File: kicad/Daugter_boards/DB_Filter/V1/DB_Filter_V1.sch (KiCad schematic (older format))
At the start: 4 parts, among them P1 CONN_01X19

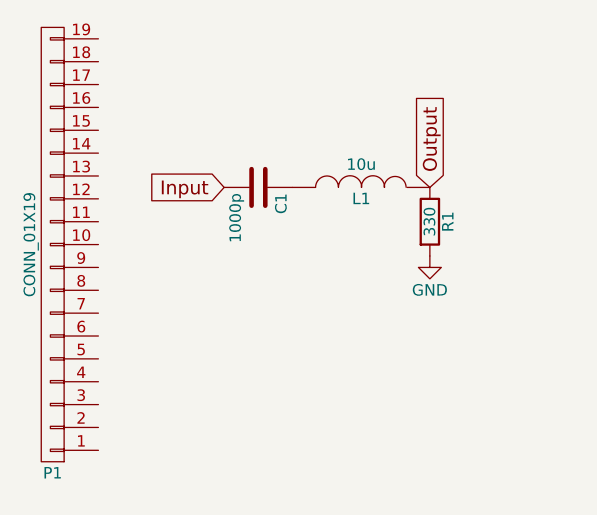
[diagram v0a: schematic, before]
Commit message: adding DB_Filter
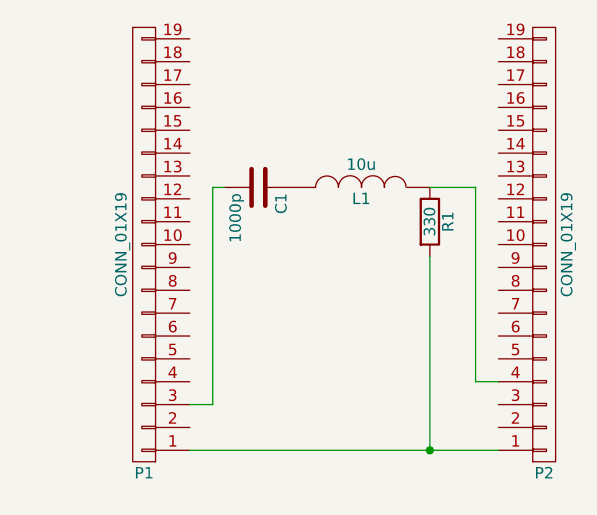
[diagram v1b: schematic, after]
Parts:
- added P2: CONN_01X19, symbol CONN_01X19
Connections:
- net GND is gone; now on an unnamed net: R1.2
- net Input is gone; now on an unnamed net: C1.2
- net at P1.1 (P1): now also P2.1 (P1)
- net Output: no longer names the net of L1.1, R1.1
- net Output: now also P2.4 (P4)
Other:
- moved on the sheet: P1
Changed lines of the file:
@@
 LIBS:valves
 LIBS:echopen
+LIBS:DB_Filter_V1-cache
 EELAYER 25 0
 EELAYER END
@@
 $EndComp
 $Comp
-L GND #PWR1
-U 1 1 57A4BBE1
-P 5350 3450
-F 0 "#PWR1" H 5350 3200 50  0001 C CNN
-F 1 "GND" H 5350 3300 50  0000 C CNN
-F 2 "" H 5350 3450 50  0000 C CNN
-F 3 "" H 5350 3450 50  0000 C CNN
-	1    5350 3450
-	1    0    0    -1
-$EndComp
-Text GLabel 4450 3150 0    60   Input ~ 0
-Input
-Text GLabel 5350 3150 1    60   Input ~ 0
-Output
-$Comp
 L CONN_01X19 P1
 U 1 1 57A84EF6
-P 3700 3400
-F 0 "P1" H 3700 4400 50  0000 C CNN
-F 1 "CONN_01X19" V 3800 3400 50  0000 C CNN
-F 2 "" H 3700 3400 50  0000 C CNN
-F 3 "" H 3700 3400 50  0000 C CNN
-	1    3700 3400
+P 4100 3400
+F 0 "P1" H 4100 4400 50  0000 C CNN
+F 1 "CONN_01X19" V 4200 3400 50  0000 C CNN
+F 2 "" H 4100 3400 50  0000 C CNN
+F 3 "" H 4100 3400 50  0000 C CNN
+	1    4100 3400
 	-1   0    0    1
 $EndComp
+$Comp
+L CONN_01X19 P2
+U 1 1 57A89932
+P 5850 3400
+F 0 "P2" H 5850 4400 50  0000 C CNN
+F 1 "CONN_01X19" V 5950 3400 50  0000 C CNN
+F 2 "" H 5850 3400 50  0000 C CNN
+F 3 "" H 5850 3400 50  0000 C CNN
+	1    5850 3400
+	1    0    0    1
+$EndComp
+Wire Wire Line
+	4300 4300 5650 4300
+Wire Wire Line
+	5350 3450 5350 4300
+Connection ~ 5350 4300
+Wire Wire Line
+	5350 3150 5550 3150
+Wire Wire Line
+	5550 3150 5550 4000
+Wire Wire Line
+	4400 3150 4400 4100
+Wire Wire Line
+	4400 3150 4450 3150
+Wire Wire Line
+	5550 4000 5650 4000
+Wire Wire Line
+	4400 4100 4300 4100
 $EndSCHEMATC

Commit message: adding DB_Filter
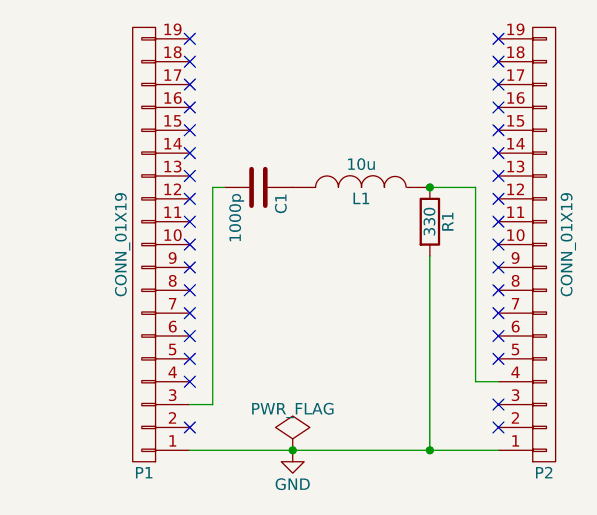
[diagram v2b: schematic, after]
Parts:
- C1: footprint (none) -> Capacitors_ThroughHole:C_Disc_D6_P5
- L1: footprint (none) -> Inductors:INDUCTOR_V
- P1, P2: footprint (none) -> Socket_Strips:Socket_Strip_Straight_1x19
- R1: footprint (none) -> Resistors_ThroughHole:Resistor_Horizontal_RM7mm
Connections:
- net GND: now reaches P1.1 (P1), P2.1 (P1), R1.2
- no-connect marks 0 -> 34
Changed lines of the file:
@@
 F 0 "C1" H 4625 3250 50  0000 L CNN
 F 1 "1000p" H 4625 3050 50  0000 L CNN
-F 2 "" H 4638 3000 50  0000 C CNN
+F 2 "Capacitors_ThroughHole:C_Disc_D6_P5" H 4638 3000 50  0001 C CNN
 F 3 "" H 4600 3150 50  0000 C CNN
 	1    4600 3150
@@
 F 0 "L1" V 5000 3150 50  0000 C CNN
 F 1 "10u" V 5150 3150 50  0000 C CNN
-F 2 "" H 5050 3150 50  0000 C CNN
+F 2 "Inductors:INDUCTOR_V" H 5050 3150 50  0001 C CNN
 F 3 "" H 5050 3150 50  0000 C CNN
 	1    5050 3150
@@
 F 0 "R1" V 5430 3300 50  0000 C CNN
 F 1 "330" V 5350 3300 50  0000 C CNN
-F 2 "" V 5280 3300 50  0000 C CNN
+F 2 "Resistors_ThroughHole:Resistor_Horizontal_RM7mm" V 5280 3300 50  0001 C CNN
 F 3 "" H 5350 3300 50  0000 C CNN
 	1    5350 3300
@@
 F 0 "P1" H 4100 4400 50  0000 C CNN
 F 1 "CONN_01X19" V 4200 3400 50  0000 C CNN
-F 2 "" H 4100 3400 50  0000 C CNN
+F 2 "Socket_Strips:Socket_Strip_Straight_1x19" H 4100 3400 50  0001 C CNN
 F 3 "" H 4100 3400 50  0000 C CNN
 	1    4100 3400
@@
 F 0 "P2" H 5850 4400 50  0000 C CNN
 F 1 "CONN_01X19" V 5950 3400 50  0000 C CNN
-F 2 "" H 5850 3400 50  0000 C CNN
+F 2 "Socket_Strips:Socket_Strip_Straight_1x19" H 5850 3400 50  0001 C CNN
 F 3 "" H 5850 3400 50  0000 C CNN
 	1    5850 3400
@@
 Wire Wire Line
 	4400 4100 4300 4100
+Connection ~ 5350 3150
+NoConn ~ 4300 2500
+NoConn ~ 4300 2600
+NoConn ~ 4300 2700
+NoConn ~ 4300 2800
+NoConn ~ 4300 2900
+NoConn ~ 4300 3000
+NoConn ~ 4300 3100
+NoConn ~ 4300 3200
+NoConn ~ 4300 3300
+NoConn ~ 4300 3400
+NoConn ~ 4300 3500
+NoConn ~ 4300 3600
+NoConn ~ 4300 3700
+NoConn ~ 4300 3800
+NoConn ~ 4300 3900
+NoConn ~ 4300 4000
+NoConn ~ 4300 4200
+NoConn ~ 5650 2500
+NoConn ~ 5650 2600
+NoConn ~ 5650 2700
+NoConn ~ 5650 2800
+NoConn ~ 5650 2900
+NoConn ~ 5650 3000
+NoConn ~ 5650 3100
+NoConn ~ 5650 3200
+NoConn ~ 5650 3300
+NoConn ~ 5650 3400
+NoConn ~ 5650 3500
+NoConn ~ 5650 3600
+NoConn ~ 5650 3700
+NoConn ~ 5650 3800
+NoConn ~ 5650 3900
+NoConn ~ 5650 4100
+NoConn ~ 5650 4200
+$Comp
+L PWR_FLAG #FLG01
+U 1 1 57AC9F7F
+P 4750 4300
+F 0 "#FLG01" H 4750 4395 50  0001 C CNN
+F 1 "PWR_FLAG" H 4750 4480 50  0000 C CNN
+F 2 "" H 4750 4300 50  0000 C CNN
+F 3 "" H 4750 4300 50  0000 C CNN
+	1    4750 4300
+	1    0    0    -1
+$EndComp
+$Comp
+L GND #PWR02
+U 1 1 57AC9FA2
+P 4750 4300
+F 0 "#PWR02" H 4750 4050 50  0001 C CNN
+F 1 "GND" H 4750 4150 50  0000 C CNN
+F 2 "" H 4750 4300 50  0000 C CNN
+F 3 "" H 4750 4300 50  0000 C CNN
+	1    4750 4300
+	1    0    0    -1
+$EndComp
+Connection ~ 4750 4300
 $EndSCHEMATC
